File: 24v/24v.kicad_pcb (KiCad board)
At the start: 2 copper layers, 55.9 x 67.3 mm, 53 parts, among them J1 Conn_01x08_Female, J2 Conn_01x01, J3 Conn_02x08_Counter_Clockwise, J4 Conn_02x08_Counter_Clockwise, J5 Conn_01x01, J6 Conn_02x08_Counter_Clockwise, J7 Conn_02x08_Counter_Clockwise, Q1 FET_A_UP, Q2 FET_A_DOWN, Q3 FET_B_UP, Q4 FET_B_DOWN, U1 7400, U2 IRS2302, U3 TLP2955, U4 TLP2955, U5 IRS2302, U6 LM7812_TO220

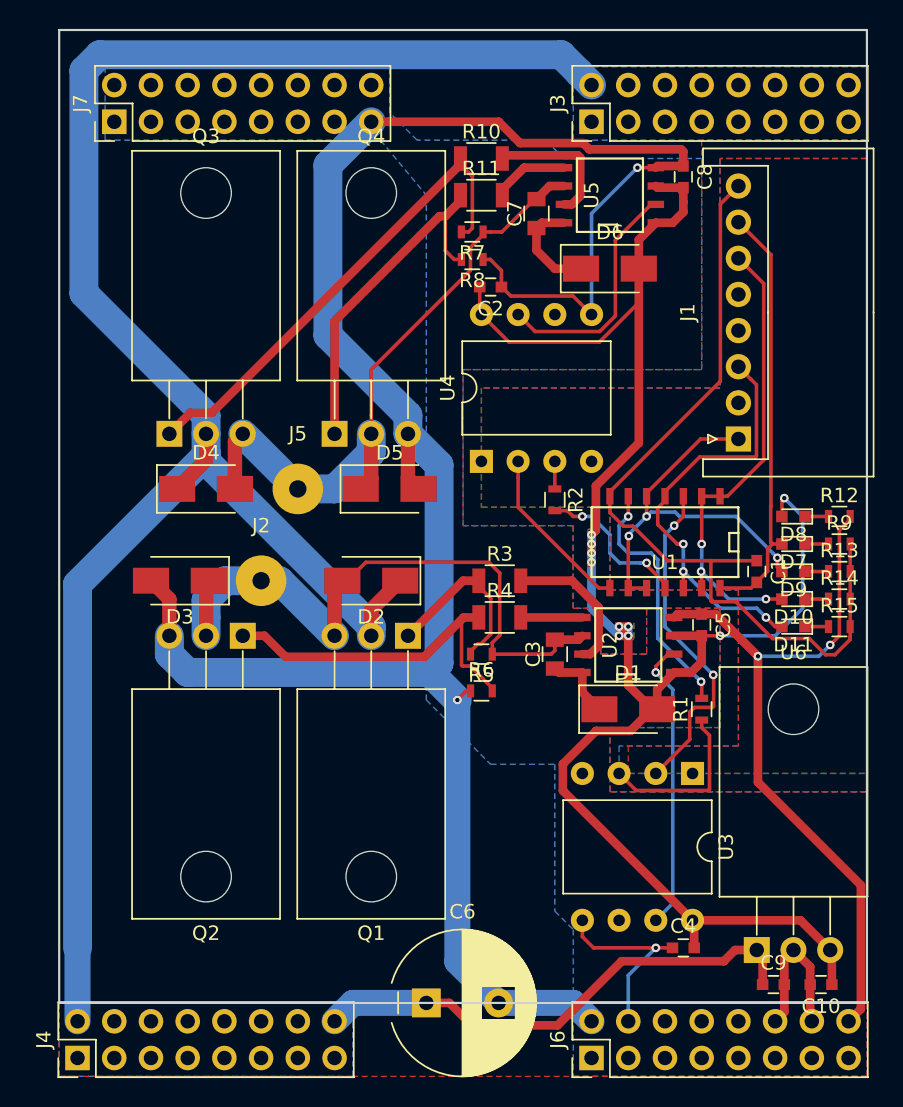
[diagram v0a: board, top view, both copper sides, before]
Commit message: fix outline
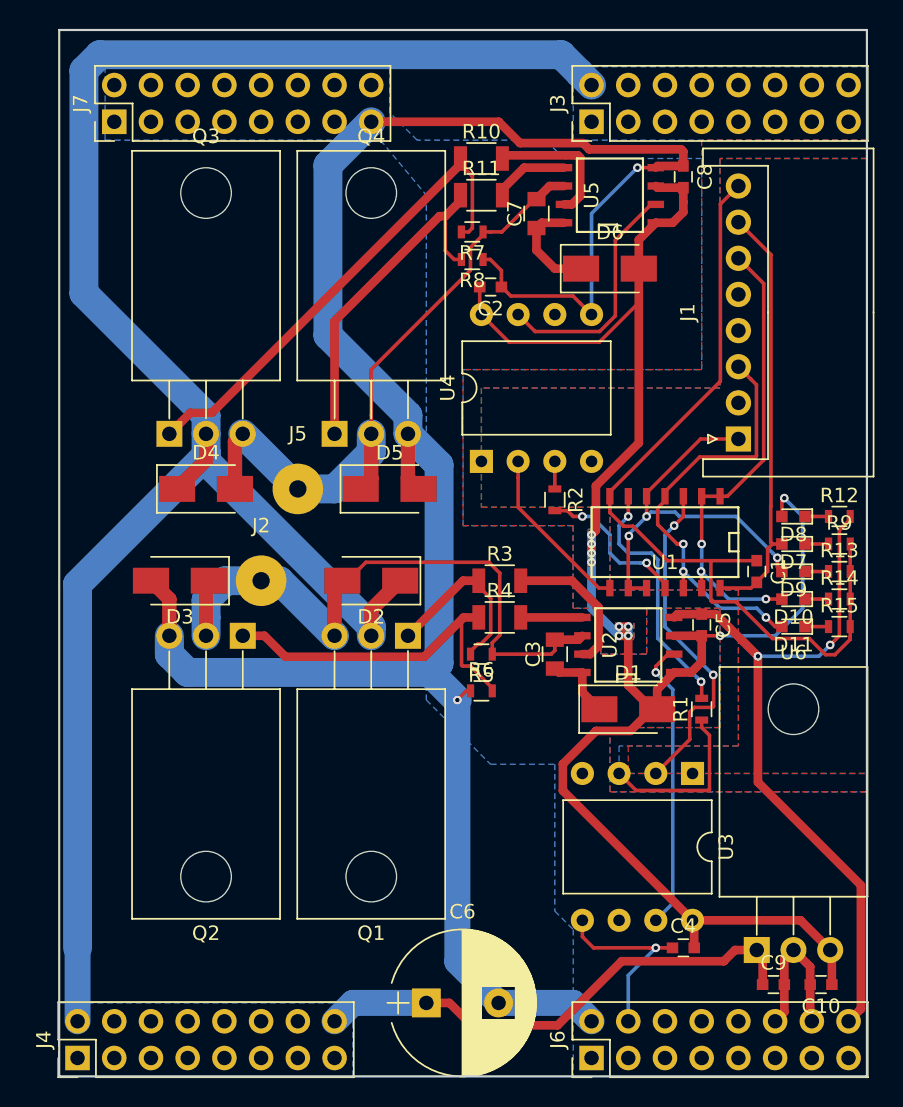
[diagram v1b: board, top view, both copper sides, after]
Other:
- board size 55.9 x 67.3 mm -> 55.9 x 72.4 mm
